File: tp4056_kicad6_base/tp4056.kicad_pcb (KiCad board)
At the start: 2 copper layers, 41.8 x 20.5 mm, 21 parts, among them J1 USB_B_Micro, J2 Conn_01x01_Female, J3 Conn_01x01_Female, J4 Conn_01x01_Female, J5 Conn_01x01_Female, J6 Conn_01x01_Female, J7 Conn_01x01_Female, U1 TP4056, U2 DW01, U3 FS8205A

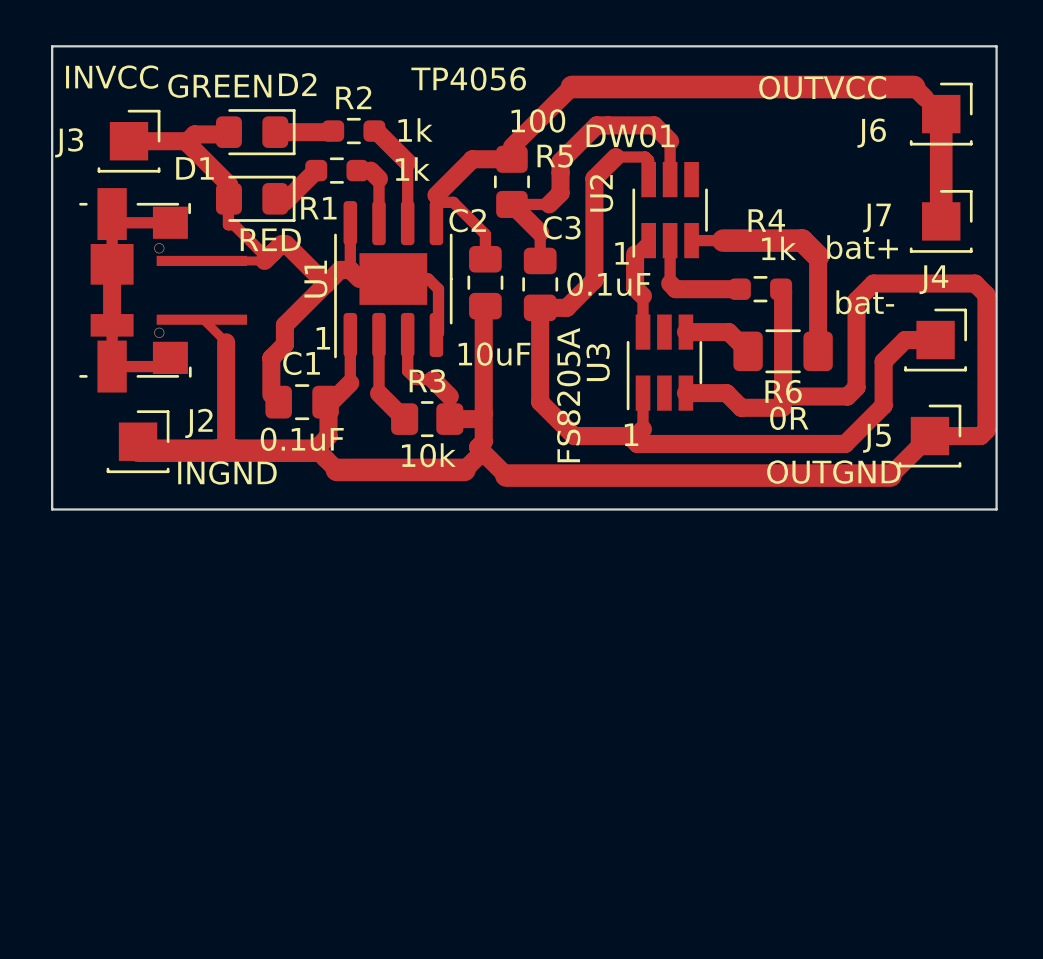
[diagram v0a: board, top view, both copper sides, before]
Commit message: add 3v3 regulator
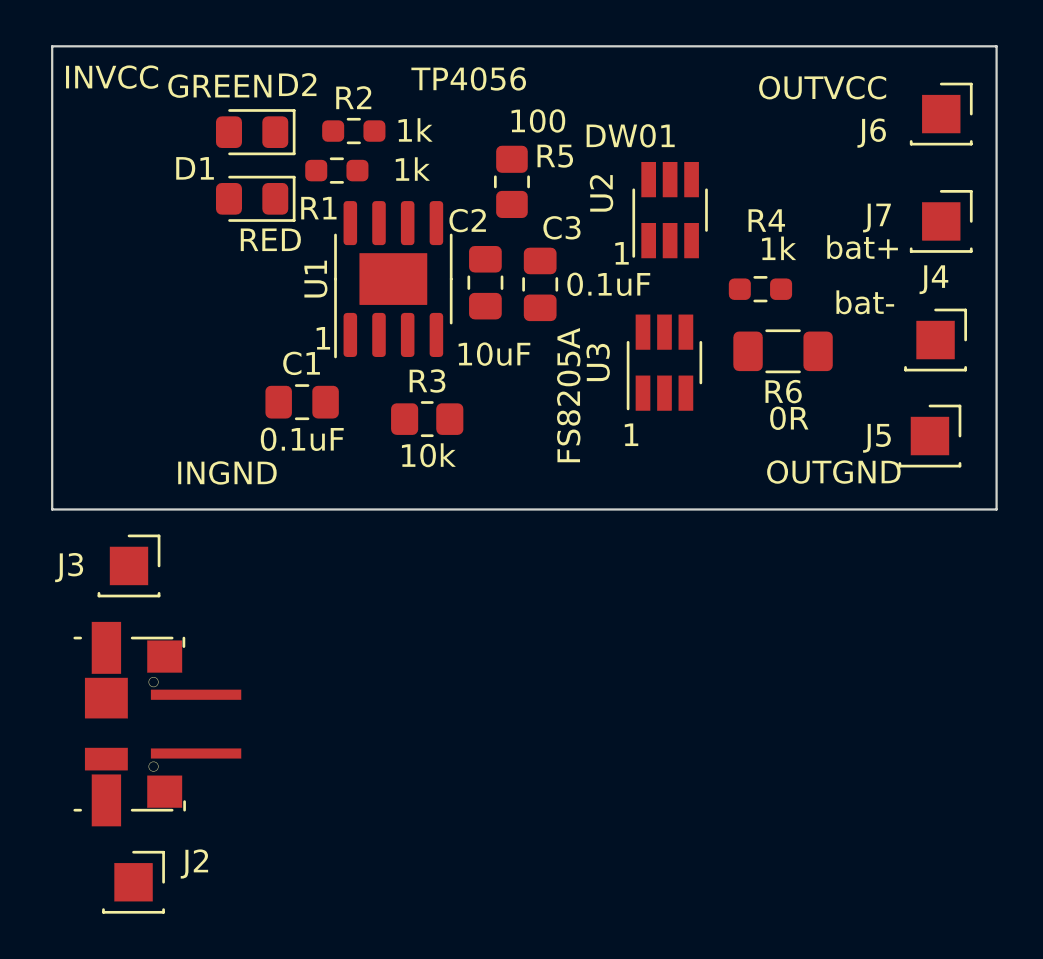
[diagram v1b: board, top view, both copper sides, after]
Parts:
- moved J2 19.5 mm to (147.0, 109.0)
- moved J1 19.2 mm to (147.0, 102.0)
- moved J3 18.8 mm to (146.8, 95.0)
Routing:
- net GND: track 94.9 -> 0.12 mm
- net BAT-: track 38.9 -> 0.00 mm
- net BAT+: track 35.0 -> 0.00 mm
- net VIN: track 34.2 -> 0.00 mm
- net Net-(C3-Pad1): track 14.3 -> 0.00 mm
- net unconnected-(J1-Pad6): track 12.2 -> 0.00 mm
- net /OC: track 10.1 -> 0.00 mm
- net Net-(R4-Pad2): track 5.09 -> 0.00 mm
- net Net-(R2-Pad2): track 4.74 -> 0.00 mm
- net /G1: track 4.44 -> 0.00 mm
- net Net-(R3-Pad1): track 4.20 -> 0.00 mm
- net /G2: track 3.10 -> 0.00 mm
- net Net-(R1-Pad2): track 3.06 -> 0.00 mm
- net Net-(D2-Pad1): track 2.58 -> 0.07 mm
- net Net-(D1-Pad1): track 2.45 -> 0.00 mm

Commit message: Add 3.3V LDO regulator
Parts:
- added C4: 10uF, Capacitor_SMD:C_0805_2012Metric_Pad1.18x1.45mm_HandSolder, F.Cu at (197.0, 83.0)
- added C5: 1uF, Capacitor_SMD:C_0805_2012Metric_Pad1.18x1.45mm_HandSolder, F.Cu at (203.8, 78.5)
- added C6: 1uF, Capacitor_SMD:C_0805_2012Metric_Pad1.18x1.45mm_HandSolder, F.Cu at (196.4, 86.3)
- added D3: MBR1020VL, Diode_SMD:D_SOD-123F, F.Cu at (191.0, 83.2)
- added Q1: FDN340P, Package_TO_SOT_SMD:SOT-23, F.Cu at (191.9, 92.0)
- added Q2: FS8205A, Package_TO_SOT_SMD_AKL:TSOT-23-6_HandSoldering, F.Cu at (192.0, 77.0)
- added R6: 100k, Resistor_SMD:R_0805_2012Metric_Pad1.20x1.40mm_HandSolder, F.Cu at (206.5, 81.5)
- added R7: 100k, Resistor_SMD:R_0805_2012Metric_Pad1.20x1.40mm_HandSolder, F.Cu at (201.2, 86.0)
- added R8: 100k, Resistor_SMD:R_0805_2012Metric_Pad1.20x1.40mm_HandSolder, F.Cu at (201.8, 83.0)
- added R9: 100k, Resistor_SMD:R_0805_2012Metric_Pad1.20x1.40mm_HandSolder, F.Cu at (208.5, 78.5)
- added U4: AP2127K-3.3, Package_TO_SOT_SMD:SOT-23-5, F.Cu at (198.0, 70.0)
- moved J1 20.0 mm to (146.0, 82.0)
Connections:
- net VIN renamed VBUS
- C1 pad 2: GND -> Earth
- C2 pad 1: BAT+ -> /BAT+
- C2 pad 2: GND -> Earth
- C3 pad 2: BAT- -> Earth
- J1 pad 5: GND -> Earth
- J2 pad 1: GND -> Earth
- J4 pad 1: BAT- -> /BAT-
- J5 pad 1: GND -> Earth
- J6 pad 1: BAT+ -> /BAT+
- J7 pad 1: BAT+ -> /OUT+
- R3 pad 2: GND -> Earth
- R4 pad 1: GND -> Earth
- R5 pad 1: BAT+ -> /BAT+
- U1 pad 1: GND -> Earth
- U1 pad 3: GND -> Earth
- U1 pad 5: BAT+ -> /BAT+
- U2 pad 1: /G1 -> Net-(Q2-Pad6)
- U2 pad 3: /OC -> Net-(Q2-Pad4)
- U2 pad 6: BAT- -> Earth

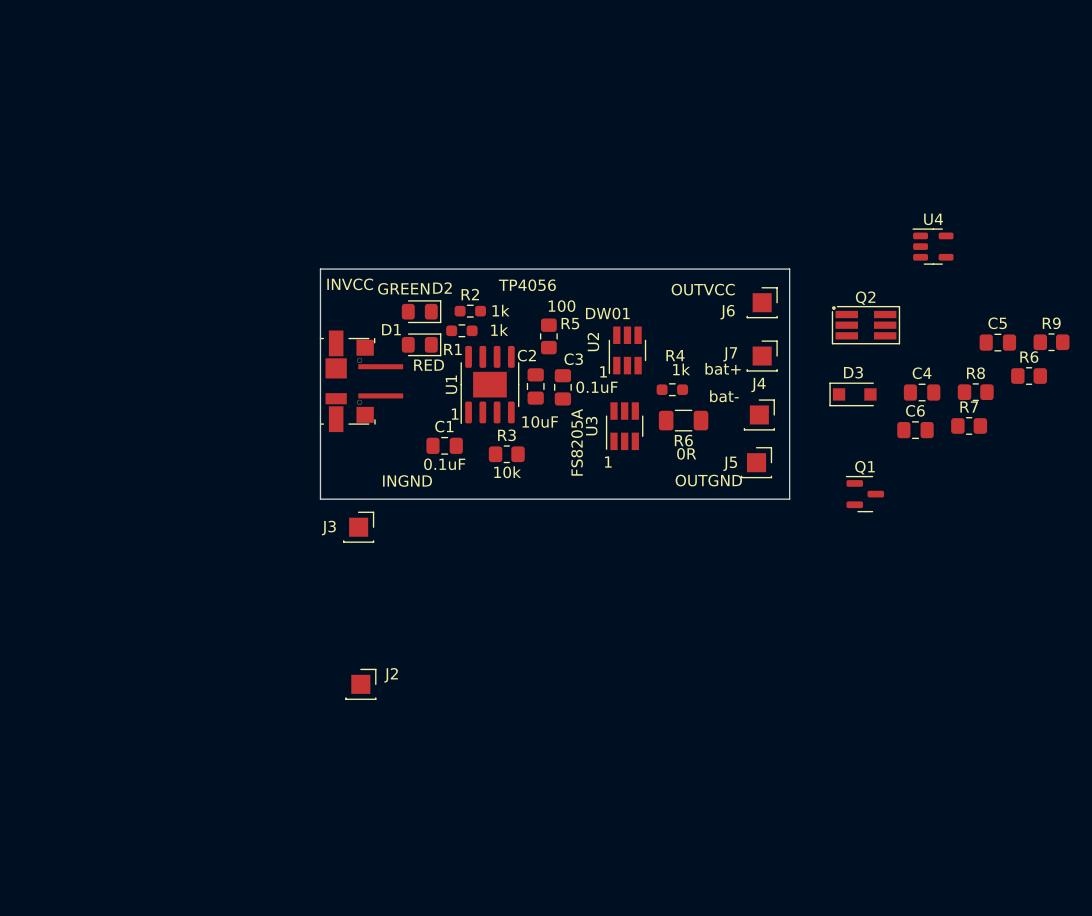
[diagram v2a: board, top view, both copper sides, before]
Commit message: pcd.Add board and position elements
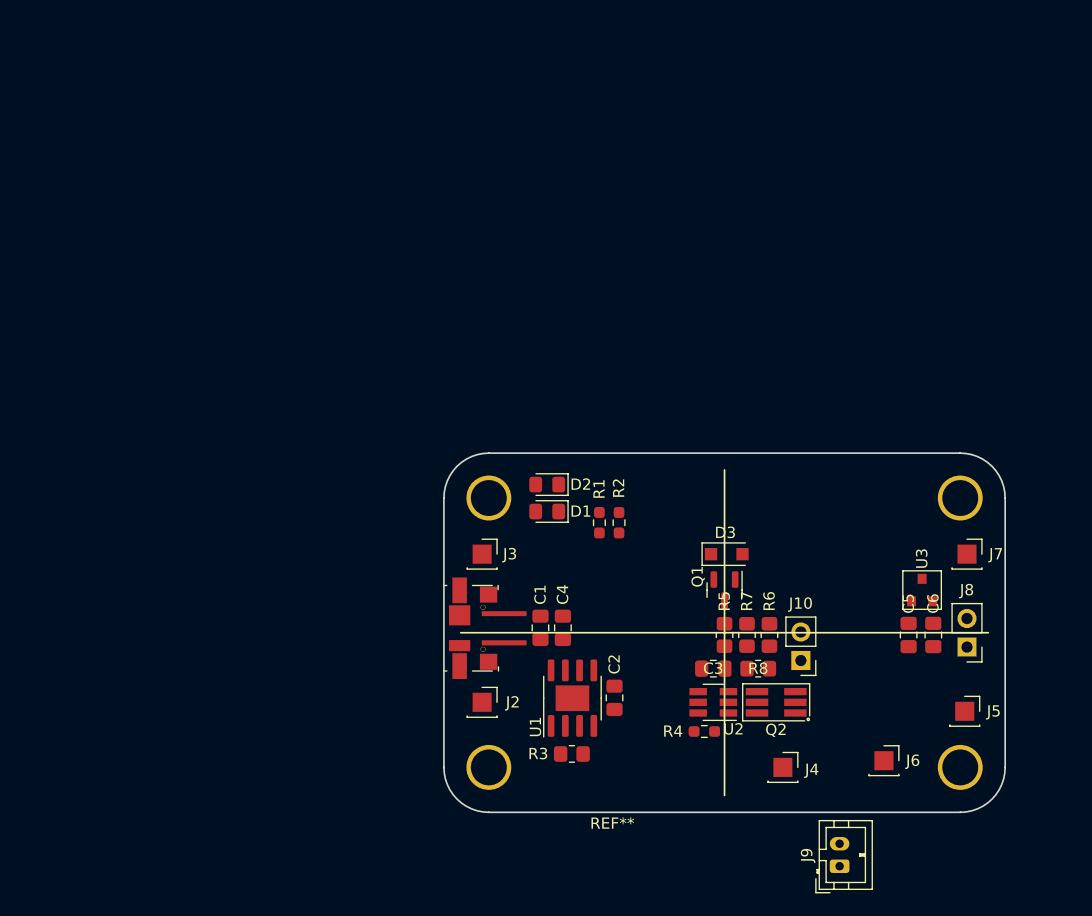
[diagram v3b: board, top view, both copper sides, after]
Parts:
- removed the R6 at (175.8, 85.5)
- removed R9: 100k, Resistor_SMD:R_0805_2012Metric_Pad1.20x1.40mm_HandSolder
- removed U4: AP2127K-3.3, Package_TO_SOT_SMD:SOT-23-5
- added J10: Conn_01x02_Male, Connector_PinHeader_2.54mm:PinHeader_1x02_P2.54mm_Vertical, F.Cu at (186.2, 106.9)
- added J8: Conn_01x02_Male, Connector_PinHeader_2.54mm:PinHeader_1x02_P2.54mm_Vertical, F.Cu at (201.0, 105.7)
- added J9: Conn_01x02_Male, Connector_JST:JST_PH_B2B-PH-K_1x02_P2.00mm_Vertical, F.Cu at (189.7, 125.2)
- added REF**: SoBr_5032, SoBr:SoBr_5032, F.Cu at (154.4, 120.4)
- D1: value RED -> LED 0805 Rojo
- D2: value GREEN -> LED 0803 Verde
- U3: value FS8205A -> LM1117-3.3; footprint Package_TO_SOT_SMD:SOT-23-6_Handsoldering -> Package_TO_SOT_SMD_AKL:SOT-23
- moved J6 42.2 mm to (193.6, 115.8)
- moved C4 38.3 mm to (165.0, 104.0), turned to -90 degrees
- moved Q2 34.5 mm to (184.0, 110.6), turned to 180 degrees
- moved R6 32.7 mm to (183.4, 104.6), turned to -90 degrees
- moved U2 32.3 mm to (178.4, 110.6), turned to 180 degrees
- moved J4 31.5 mm to (184.6, 116.4)
- moved R8 31.3 mm to (182.4, 107.6)
- moved R5 30.9 mm to (179.4, 104.6)
- moved R4 30.6 mm to (177.6, 113.2), turned to 0 degrees
- moved U3 30.3 mm to (197.0, 100.6)
- moved J5 28.9 mm to (200.8, 111.4)
- moved U1 28.9 mm to (165.8, 110.2)
- moved C2 28.6 mm to (169.6, 110.2)
- moved C3 28.4 mm to (178.4, 107.6), turned to 180 degrees
- moved R3 27.3 mm to (165.8, 115.2)
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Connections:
- U3 pad 1: BAT- -> Earth
- U3 pad 2: unconnected-(U3-Pad2) -> Net-(C6-Pad1)
- U3 pad 3: GND -> /OUT+
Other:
- board size 41.8 x 20.5 mm -> 50 x 32 mm
- board text removed: "1"
- board text removed: "INGND"
- board text removed: "INVCC"
- board text removed: "OUTGND"
- board text removed: "OUTVCC"
- board text removed: "bat+"
- board text removed: "bat-"

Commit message: pcb. Board ready in 4032
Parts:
- REF**: value SoBr_5032 -> SoBr_4032; footprint SoBr:SoBr_5032 -> SoBr:SoBr_4032
- moved J5 28.3 mm to (179.8, 92.4)
- moved J7 25.3 mm to (176.2, 92.4)
- moved C6 21.6 mm to (176.8, 100.6), turned to 180 degrees
- moved C5 21.3 mm to (176.8, 95.0), turned to 0 degrees
- moved U3 20.4 mm to (176.8, 97.8)
- moved J8 20.2 mm to (181.6, 100.1)
- moved R6 16.1 mm to (172.4, 92.8), turned to 0 degrees
- moved J9 14.6 mm to (178.4, 115.8), turned to 0 degrees
- moved J4 10.4 mm to (174.2, 116.4)
- moved J6 9.02 mm to (184.6, 116.4)
- moved Q1 8.49 mm to (172.4, 95.8), turned to 90 degrees
- moved D3 7.38 mm to (172.4, 99.0), turned to 180 degrees
- moved C2 5.66 mm to (172.6, 105.4)
- moved U1 5.49 mm to (168.8, 105.6)
- moved J10 4.69 mm to (181.6, 107.8)
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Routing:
- net Earth: track 0.00 -> 127.2 mm
- net VBUS: track 0.00 -> 46.4 mm
- net /BAT+: track 0.00 -> 33.9 mm, vias 0 -> 1
- net /OUT+: track 0.00 -> 10.5 mm
- net /BAT-: track 0.00 -> 10.1 mm
- net /measurment: track 0.00 -> 7.27 mm
- net Net-(D2-Pad1): track 0.00 -> 6.76 mm
- net Net-(C3-Pad1): track 0.00 -> 6.36 mm
- net Net-(C6-Pad1): track 0.00 -> 6.18 mm
- net Net-(U1-Pad7): track 0.00 -> 4.36 mm
- net Net-(U1-Pad6): track 0.00 -> 4.22 mm
- net Net-(R4-Pad2): track 0.00 -> 4.07 mm
- net Net-(D1-Pad1): track 0.00 -> 3.59 mm
- net Net-(Q2-Pad2): track 0.00 -> 3.42 mm
- net Net-(Q2-Pad6): track 0.00 -> 2.54 mm
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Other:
- board size 50 x 32 mm -> 40 x 32 mm

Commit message: pcb. Board 38x18
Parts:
- removed REF**: SoBr_4032, SoBr:SoBr_4032
- J1: footprint usb_footprint:tp4056_USB_Micro-B_Molex_47346-0001_fix -> Connector_USB:USB_Micro-B_Molex-105017-0001
- moved J9 65.2 mm to (161.0, 53.0), turned to 180 degrees
- moved J6 55.9 mm to (165.0, 64.0)
- moved J4 52.7 mm to (169.0, 64.0)
- moved Q2 43.5 mm to (169.0, 69.0), turned to -90 degrees
- moved R4 39.8 mm to (172.0, 74.0), turned to 90 degrees
- moved J10 37.8 mm to (183.0, 70.0)
- moved R7 37.5 mm to (179.0, 68.0)
- moved C2 37.2 mm to (165.0, 69.0)
- moved U2 37.0 mm to (169.0, 74.5), turned to -90 degrees
- moved R3 36.5 mm to (160.0, 76.0), turned to 0 degrees
- moved R8 36.4 mm to (179.0, 72.0), turned to -90 degrees
- moved C4 36.1 mm to (156.0, 69.0)
- moved C1 36.1 mm to (154.0, 69.0)
- moved U1 35.7 mm to (160.0, 71.0)
- moved R2 35.6 mm to (159.0, 64.0), turned to 0 degrees
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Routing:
- net Earth: track 127.2 -> 86.5 mm
- net /BAT+: track 33.9 -> 12.2 mm, vias 1 -> 0
- net VBUS: track 46.4 -> 28.5 mm
- net /BAT-: track 10.1 -> 3.68 mm
- net Net-(D2-Pad1): track 6.76 -> 2.06 mm
- net Net-(C3-Pad1): track 6.36 -> 2.83 mm
- net /OUT+: track 10.5 -> 12.3 mm
- net Net-(R1-Pad2): track 4.36 -> 2.75 mm
- net Net-(R2-Pad2): track 4.22 -> 5.75 mm
- net Net-(D1-Pad1): track 3.59 -> 2.06 mm
- net Net-(C6-Pad1): track 6.18 -> 7.21 mm
- net /measurment: track 7.27 -> 6.64 mm
- net Net-(R4-Pad2): track 4.07 -> 4.66 mm
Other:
- board size 40 x 32 mm -> 37.5 x 17.5 mm

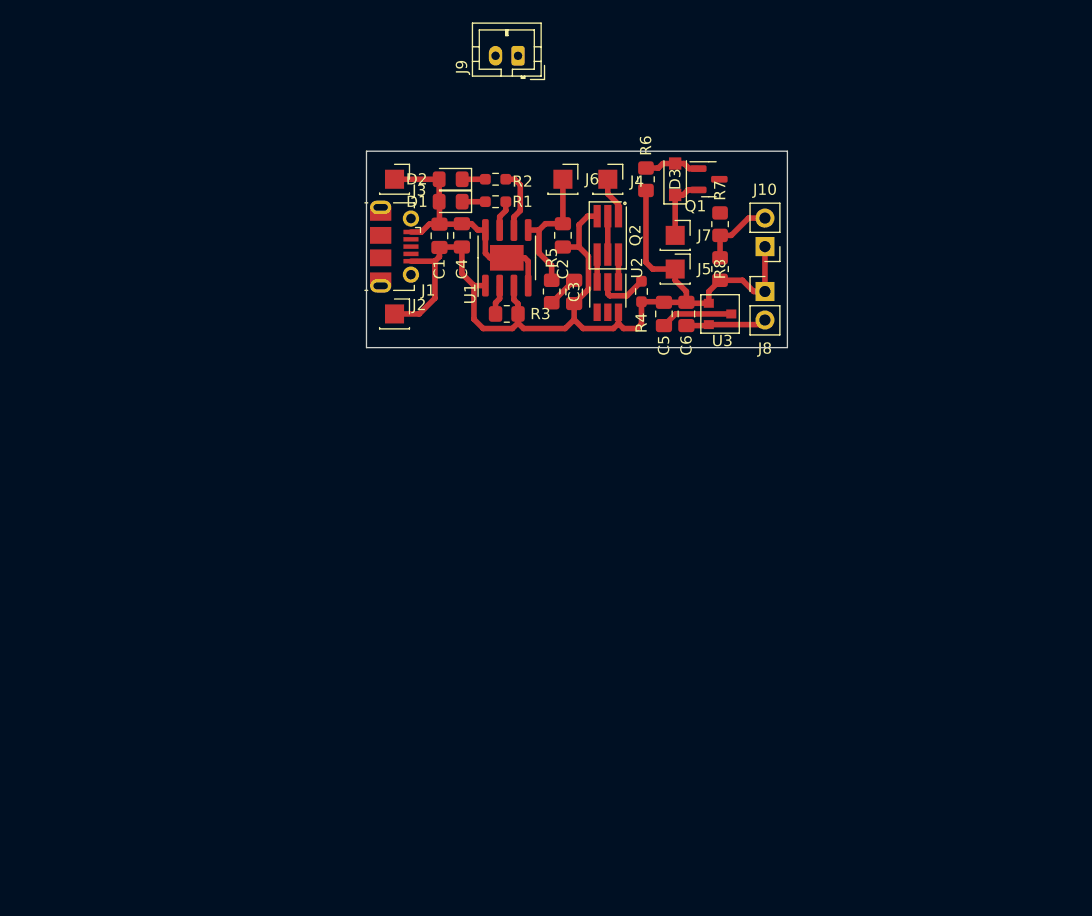
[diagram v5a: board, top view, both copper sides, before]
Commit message: pcb. board 40x20 one layer
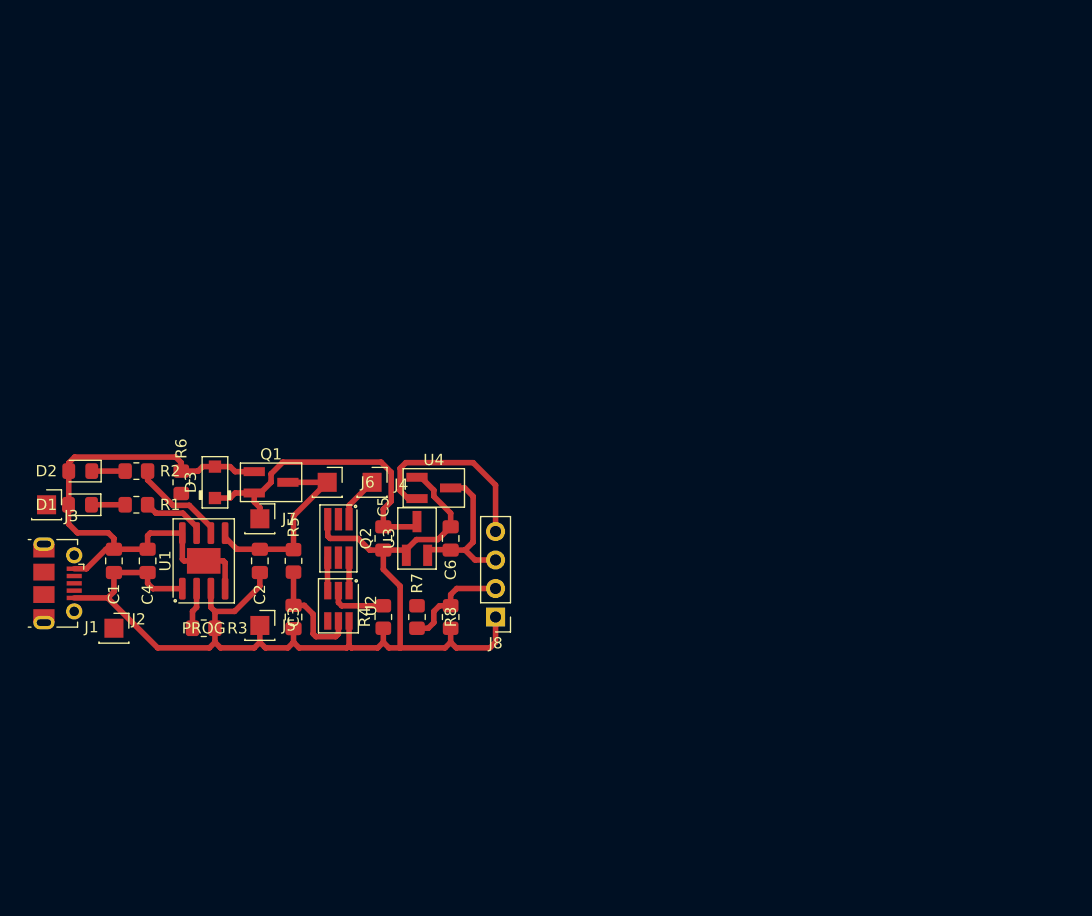
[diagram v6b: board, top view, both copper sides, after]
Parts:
- removed J10: Conn_01x02_Male, Connector_PinHeader_2.54mm:PinHeader_1x02_P2.54mm_Vertical
- removed J9: Conn_01x02_Male, Connector_JST:JST_PH_B2B-PH-K_1x02_P2.00mm_Vertical
- added U4: LM809, Package_TO_SOT_SMD_AKL:SOT-23_Handsoldering, F.Cu at (153.5, 91.5)
- C2, C4: value 10uF -> MLCC 10uF 10V 0805
- D3: footprint Diode_SMD:D_SOD-123F -> Diode_SMD_AKL:D_SOD-123F
- J8: value Conn_01x02_Male -> Conn_01x04_Male; footprint Connector_PinHeader_2.54mm:PinHeader_1x02_P2.54mm_Vertical -> Connector_PinHeader_2.54mm:PinHeader_1x04_P2.54mm_Vertical
- Q1: footprint Package_TO_SOT_SMD:SOT-23 -> Package_TO_SOT_SMD_AKL:SOT-23_Handsoldering
- R1, R2, R4: footprint Resistor_SMD:R_0603_1608Metric_Pad0.98x0.95mm_HandSolder -> Resistor_SMD:R_0805_2012Metric_Pad1.20x1.40mm_HandSolder
- U1: footprint Package_SO:SOIC-8-1EP_3.9x4.9mm_P1.27mm_EP2.29x3mm -> Package_SO_AKL:SOIC-8-1EP_3.9x4.9mm_P1.27mm_EP2.29x3mm
- U2: footprint Package_TO_SOT_SMD:SOT-23-6_Handsoldering -> Package_TO_SOT_SMD_AKL:SOT-23-6_Handsoldering
- U3: footprint Package_TO_SOT_SMD_AKL:SOT-23 -> Package_TO_SOT_SMD_AKL:SOT-23_Handsoldering
- moved R6 49.4 mm to (131.0, 91.0)
- moved D3 49.1 mm to (134.0, 91.0)
- moved J5 48.8 mm to (138.0, 103.8)
- moved Q1 47.4 mm to (139.0, 91.0)
- moved J7 44.8 mm to (138.0, 94.2)
- moved R7 44.2 mm to (152.0, 103.0)
- moved D1 42.7 mm to (122.0, 93.0)
- moved J3 42.4 mm to (119.0, 93.0)
- moved J1 42.4 mm to (120.0, 100.0)
- moved D2 42.0 mm to (122.0, 90.0)
- moved R1 41.9 mm to (127.0, 93.0)
- moved R2 41.2 mm to (127.0, 90.0)
- moved C1 41.0 mm to (125.0, 98.0)
- moved C4 40.3 mm to (128.0, 98.0)
- moved C2 39.6 mm to (138.0, 98.0)
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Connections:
- C6 pad 1: Net-(C6-Pad1) -> +3.3V
- J8 pad 2: Net-(C6-Pad1) -> /measurment
- Q2 pad 2: Net-(Q2-Pad2) -> unconnected-(Q2-Pad2)
- Q2 pad 5: Net-(Q2-Pad2) -> unconnected-(Q2-Pad5)
- U3 pad 2: Net-(C6-Pad1) -> +3.3V
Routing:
- net VBUS: track 28.5 -> 49.3 mm
- net /RST: track 0.00 -> 17.5 mm
- net /OUT+: track 12.3 -> 28.5 mm
- net Earth: track 86.5 -> 101.3 mm
- net +3.3V: track 0.00 -> 13.8 mm
- net Net-(C3-Pad1): track 2.83 -> 10.4 mm
- net Net-(C6-Pad1): track 7.21 -> 0.00 mm
- net /BAT+: track 12.2 -> 17.7 mm
- net Net-(Q2-Pad2): track 3.42 -> 0.00 mm
- net /measurment: track 6.64 -> 9.64 mm
- net Net-(R1-Pad2): track 2.75 -> 5.74 mm
- net Net-(R2-Pad2): track 5.75 -> 8.71 mm
- net Net-(R3-Pad1): track 2.68 -> 3.68 mm
- net Net-(D1-Pad1): track 2.06 -> 3.00 mm
- net Net-(D2-Pad1): track 2.06 -> 2.97 mm
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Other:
- board outline removed

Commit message: finish version 44x19mm
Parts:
- moved J2 1.41 mm to (124.0, 105.0)
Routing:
- net /BAT+: track 17.7 -> 34.0 mm, vias 0 -> 2
- net Earth: track 101.3 -> 116.5 mm, vias 0 -> 2
- net VBUS: track 49.3 -> 51.2 mm
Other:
- board outline added: 44 x 19 mm
